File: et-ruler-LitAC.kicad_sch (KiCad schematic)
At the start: 18 parts, among them J1 Conn_01x03, SW1 SW_DPST

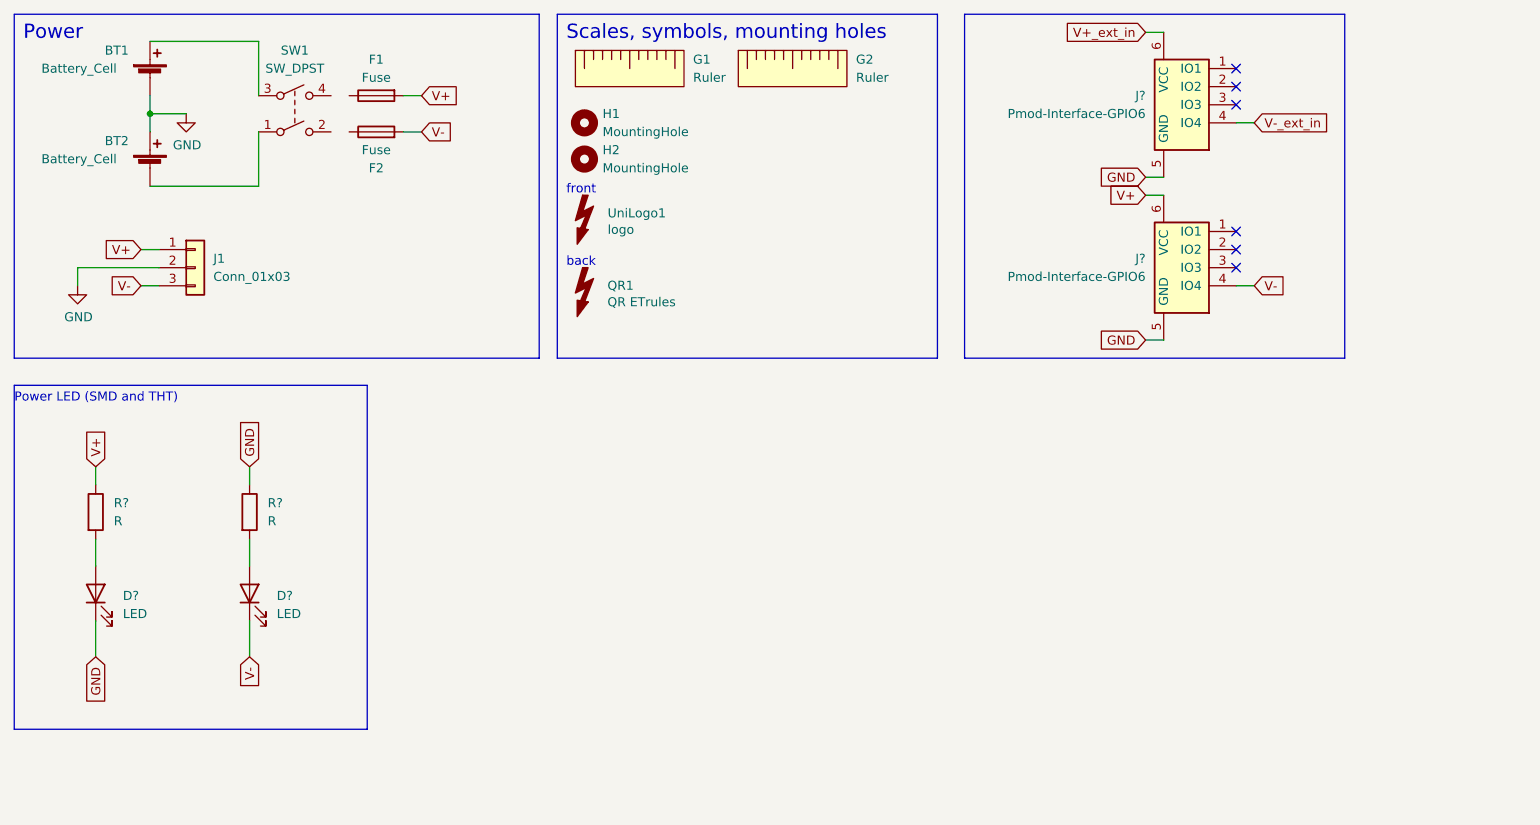
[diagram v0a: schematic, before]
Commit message: Add Converter schematic
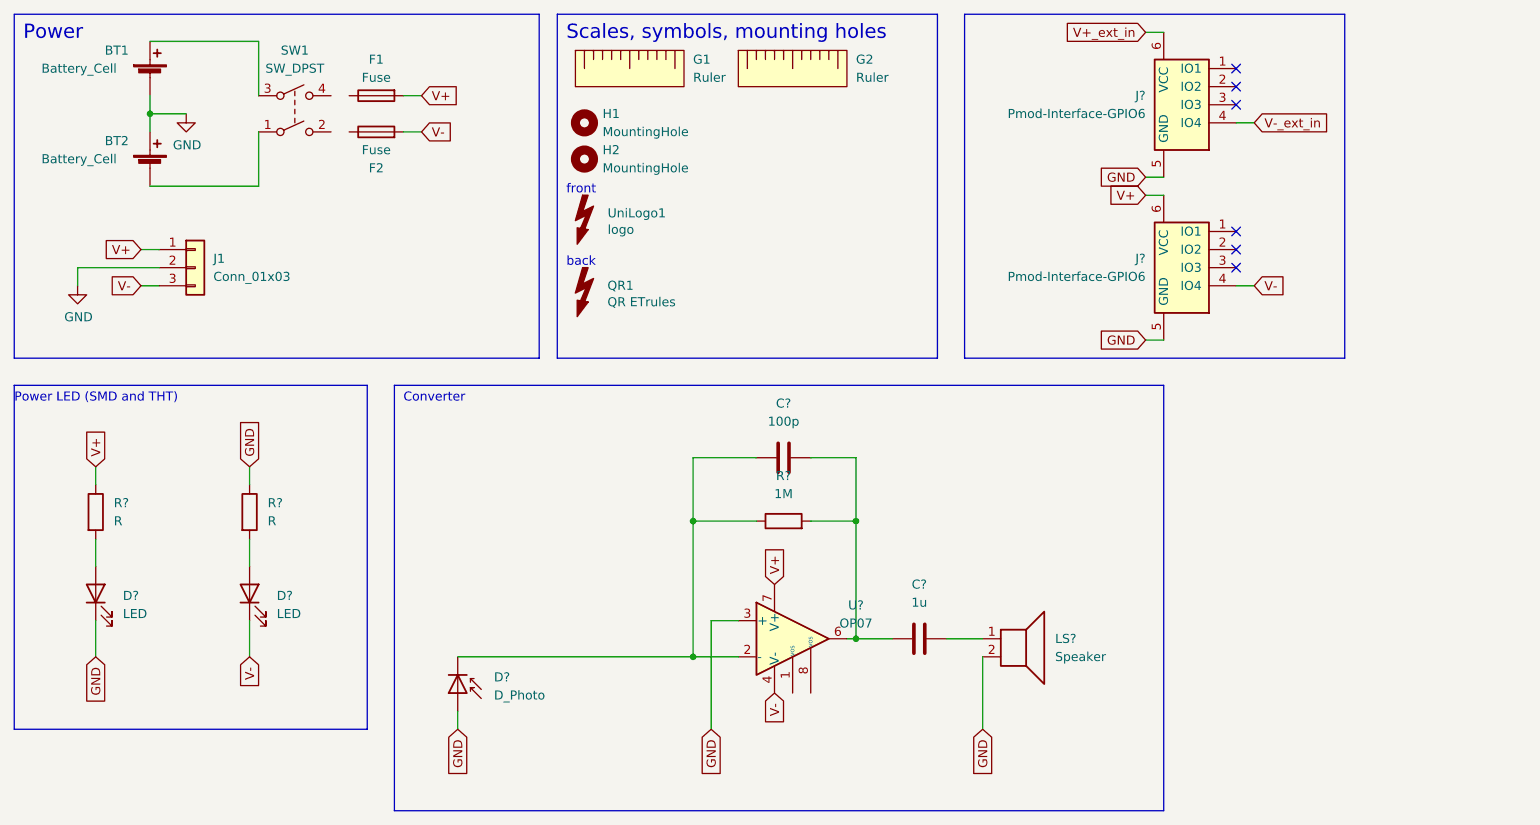
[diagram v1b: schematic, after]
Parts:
- added C?: 1u, symbol Device:C
- added C?: 100p, symbol Device:C
- added D?: D_Photo, LED_THT:LED_D5.0mm_Clear, symbol Device:D_Photo
- added LS?: Speaker, symbol Device:Speaker
- added R?: 1M, symbol Device:R
- added U?: OP07, Package_DIP:DIP-8_W7.62mm_Socket_LongPads, symbol Amplifier_Operational:OP07
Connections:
- net GND: now also D?.2 (A), LS?.2, U?.3 (+)
- net V+: now also U?.7 (V+)
- net V-: now also U?.4 (V-)
- new net: C?.1, D?.1 (K), R?.1, U?.2 (-)
- new net: C?.1, C?.2, R?.2, U?.6
- new net: C?.2, LS?.1
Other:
- note added: "Converter"

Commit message: Fix GND symbol and schematic labels
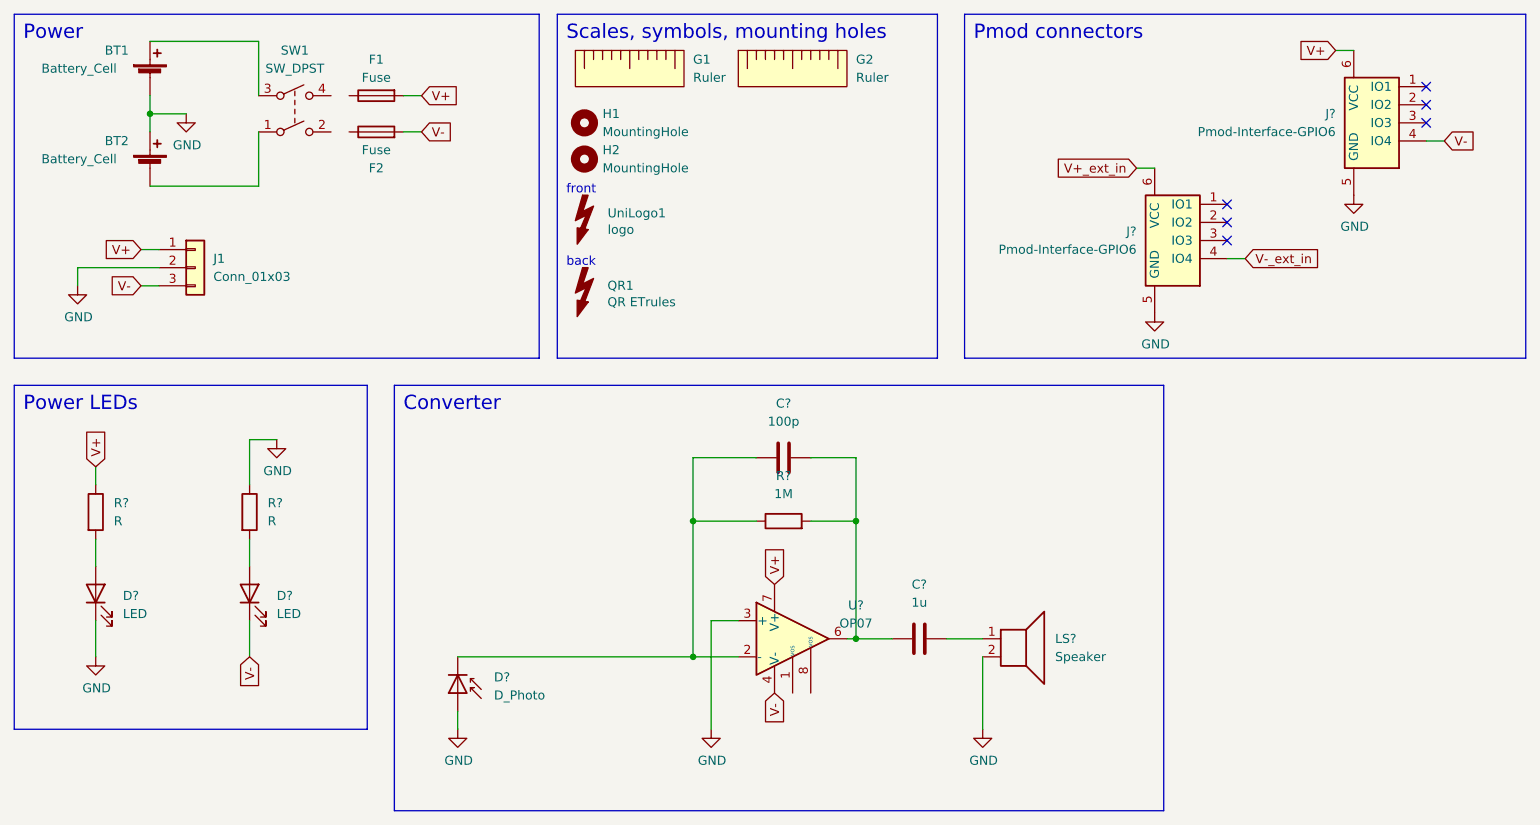
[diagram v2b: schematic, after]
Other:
- note added: "Pmod connectors"
- note added: "Power LEDs"
- note removed: "Power LED (SMD and THT)"
- moved on the sheet: J?

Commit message: Add volume control and headphone jack
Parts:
- added J?: AudioJack2, symbol Connector:AudioJack2
- added RV?: R_Potentiometer, symbol Device:R_Potentiometer
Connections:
- net GND: now also J?.T
- net at C?.2: now also RV?.1, RV?.2; no longer LS?.1
- new net: J?.S, LS?.1, RV?.3
- no-connect marks 6 -> 8
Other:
- moved on the sheet: LS?
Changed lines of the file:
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@@
   (junction (at 135.89 105.41) (diameter 0) (color 0 0 0 0)
   )
+  (junction (at 166.37 118.11) (diameter 0) (color 0 0 0 0)
+  )
+  (junction (at 168.91 105.41) (diameter 0) (color 0 0 0 0)
+  )
   (junction (at 36.83 31.75) (diameter 0) (color 0 0 0 0)
   )
   (junction (at 113.03 107.95) (diameter 0) (color 0 0 0 0)
   )
+  (junction (at 151.13 105.41) (diameter 0) (color 0 0 0 0)
+  )
+  (no_connect (at 127 113.03))
   (no_connect (at 187.96 46.99))
   (no_connect (at 215.9 33.02))
+  (no_connect (at 129.54 113.03))
   (no_connect (at 215.9 30.48))
   (no_connect (at 187.96 44.45))
@@
     (stroke (width 0) (type default) (color 0 0 0 0))
   )
-  (wire (pts (xy 148.59 105.41) (xy 153.67 105.41))
-    (stroke (width 0) (type default) (color 0 0 0 0))
-  )
-  (polyline (pts (xy 71.12 129.54) (xy 179.07 129.54))
+  (polyline (pts (xy 71.12 129.54) (xy 194.31 129.54))
     (stroke (width 0) (type default) (color 0 0 0 0))
   )
@@
     (stroke (width 0) (type default) (color 0 0 0 0))
   )
-  (polyline (pts (xy 179.07 129.54) (xy 179.07 69.85))
+  (polyline (pts (xy 194.31 129.54) (xy 194.31 69.85))
     (stroke (width 0) (type default) (color 0 0 0 0))
   )
@@
     (stroke (width 0) (type default) (color 0 0 0 0))
   )
+  (wire (pts (xy 148.59 105.41) (xy 151.13 105.41))
+    (stroke (width 0) (type default) (color 0 0 0 0))
+  )
   (polyline (pts (xy 67.31 118.11) (xy 67.31 69.85))
     (stroke (width 0) (type default) (color 0 0 0 0))
@@
     (stroke (width 0) (type default) (color 0 0 0 0))
   )
+  (wire (pts (xy 166.37 118.11) (xy 172.72 118.11))
+    (stroke (width 0) (type default) (color 0 0 0 0))
+  )
   (wire (pts (xy 113.03 88.9) (xy 113.03 107.95))
     (stroke (width 0) (type default) (color 0 0 0 0))
   )
+  (wire (pts (xy 160.02 105.41) (xy 168.91 105.41))
+    (stroke (width 0) (type default) (color 0 0 0 0))
+  )
   (wire (pts (xy 80.01 115.57) (xy 80.01 118.11))
     (stroke (width 0) (type default) (color 0 0 0 0))
@@
     (stroke (width 0) (type default) (color 0 0 0 0))
   )
+  (wire (pts (xy 151.13 105.41) (xy 152.4 105.41))
+    (stroke (width 0) (type default) (color 0 0 0 0))
+  )
+  (wire (pts (xy 168.91 105.41) (xy 172.72 105.41))
+    (stroke (width 0) (type default) (color 0 0 0 0))
+  )
   (wire (pts (xy 134.62 105.41) (xy 135.89 105.41))
     (stroke (width 0) (type default) (color 0 0 0 0))
@@
     (stroke (width 0) (type default) (color 0 0 0 0))
   )
+  (wire (pts (xy 166.37 107.95) (xy 166.37 118.11))
+    (stroke (width 0) (type default) (color 0 0 0 0))
+  )
   (wire (pts (xy 121.92 80.01) (xy 113.03 80.01))
     (stroke (width 0) (type default) (color 0 0 0 0))
@@
     (stroke (width 0) (type default) (color 0 0 0 0))
   )
+  (wire (pts (xy 168.91 115.57) (xy 172.72 115.57))
+    (stroke (width 0) (type default) (color 0 0 0 0))
+  )
   (wire (pts (xy 113.03 80.01) (xy 113.03 88.9))
     (stroke (width 0) (type default) (color 0 0 0 0))
@@
     (stroke (width 0) (type default) (color 0 0 0 0))
   )
+  (wire (pts (xy 166.37 107.95) (xy 172.72 107.95))
+    (stroke (width 0) (type default) (color 0 0 0 0))
+  )
   (polyline (pts (xy 93.98 17.78) (xy 147.32 17.78))
     (stroke (width 0) (type default) (color 0 0 0 0))
   )
-  (wire (pts (xy 153.67 107.95) (xy 153.67 118.11))
-    (stroke (width 0) (type default) (color 0 0 0 0))
-  )
   (wire (pts (xy 41.91 31.75) (xy 36.83 31.75))
     (stroke (width 0) (type default) (color 0 0 0 0))
@@
     (stroke (width 0) (type default) (color 0 0 0 0))
   )
+  (wire (pts (xy 151.13 101.6) (xy 156.21 101.6))
+    (stroke (width 0) (type default) (color 0 0 0 0))
+  )
   (polyline (pts (xy 147.32 66.04) (xy 147.32 17.78))
     (stroke (width 0) (type default) (color 0 0 0 0))
@@
     (stroke (width 0) (type default) (color 0 0 0 0))
   )
+  (wire (pts (xy 166.37 118.11) (xy 166.37 120.65))
+    (stroke (width 0) (type default) (color 0 0 0 0))
+  )
   (wire (pts (xy 36.83 21.59) (xy 52.07 21.59))
     (stroke (width 0) (type default) (color 0 0 0 0))
   )
+  (wire (pts (xy 151.13 105.41) (xy 151.13 101.6))
+    (stroke (width 0) (type default) (color 0 0 0 0))
+  )
   (wire (pts (xy 135.89 88.9) (xy 135.89 105.41))
     (stroke (width 0) (type default) (color 0 0 0 0))
   )
-  (polyline (pts (xy 179.07 69.85) (xy 71.12 69.85))
+  (polyline (pts (xy 194.31 69.85) (xy 71.12 69.85))
     (stroke (width 0) (type default) (color 0 0 0 0))
   )
   (wire (pts (xy 26.67 55.88) (xy 26.67 53.34))
+    (stroke (width 0) (type default) (color 0 0 0 0))
+  )
+  (wire (pts (xy 168.91 105.41) (xy 168.91 115.57))
     (stroke (width 0) (type default) (color 0 0 0 0))
   )
@@
     (pin "1")
   )
-  (symbol (lib_id "power:GND") (at 153.67 118.11 0) (unit 1)
-    (in_bom yes) (on_board yes)
-    (property "Reference" "#PWR?" (id 0) (at 153.67 124.46 0)
-      (effects (font (size 1.27 1.27)) hide)
-    )
-    (property "Value" "GND" (id 1) (at 153.797 122.5042 0))
-    (property "Footprint" "" (id 2) (at 153.67 118.11 0)
-      (effects (font (size 1.27 1.27)) hide)
-    )
-    (property "Datasheet" "" (id 3) (at 153.67 118.11 0)
+  (symbol (lib_id "power:GND") (at 166.37 120.65 0) (unit 1)
+    (in_bom yes) (on_board yes)
+    (property "Reference" "#PWR?" (id 0) (at 166.37 127 0)
+      (effects (font (size 1.27 1.27)) hide)
+    )
+    (property "Value" "GND" (id 1) (at 166.497 125.0442 0))
+    (property "Footprint" "" (id 2) (at 166.37 120.65 0)
+      (effects (font (size 1.27 1.27)) hide)
+    )
+    (property "Datasheet" "" (id 3) (at 166.37 120.65 0)
       (effects (font (size 1.27 1.27)) hide)
     )
@@
     (pin "1")
   )
+  (symbol (lib_id "Connector:AudioJack2") (at 177.8 118.11 0) (mirror y) (unit 1)
+    (in_bom yes) (on_board yes) (fields_autoplaced)
+    (property "Reference" "J?" (id 0) (at 182.88 116.2049 0)
+      (effects (font (size 1.27 1.27)) (justify right))
+    )
+    (property "Value" "AudioJack2" (id 1) (at 182.88 118.7449 0)
+      (effects (font (size 1.27 1.27)) (justify right))
+    )
+    (property "Footprint" "" (id 2) (at 177.8 118.11 0)
+      (effects (font (size 1.27 1.27)) hide)
+    )
+    (property "Datasheet" "~" (id 3) (at 177.8 118.11 0)
+      (effects (font (size 1.27 1.27)) hide)
+    )
+    (pin "S")
+    (pin "T")
+  )
   (symbol (lib_id "Device:C") (at 125.73 80.01 90) (unit 1)
     (in_bom yes) (on_board yes) (fields_autoplaced)
@@
     (pin "1")
   )
+  (symbol (lib_id "Device:R_Potentiometer") (at 156.21 105.41 90) (unit 1)
+    (in_bom yes) (on_board yes) (fields_autoplaced)
+    (property "Reference" "RV?" (id 0) (at 156.21 109.22 90))
+    (property "Value" "R_Potentiometer" (id 1) (at 156.21 111.76 90))
+    (property "Footprint" "" (id 2) (at 156.21 105.41 0)
+      (effects (font (size 1.27 1.27)) hide)
+    )
+    (property "Datasheet" "~" (id 3) (at 156.21 105.41 0)
+      (effects (font (size 1.27 1.27)) hide)
+    )
+    (pin "1")
+    (pin "2")
+    (pin "3")
+  )
   (symbol (lib_id "Device:R") (at 29.21 87.63 0) (unit 1)
     (in_bom yes) (on_board yes) (fields_autoplaced)
@@
     (pin "2")
   )
-  (symbol (lib_id "Device:Speaker") (at 158.75 105.41 0) (unit 1)
-    (in_bom yes) (on_board yes) (fields_autoplaced)
-    (property "Reference" "LS?" (id 0) (at 163.83 105.4099 0)
-      (effects (font (size 1.27 1.27)) (justify left))
-    )
-    (property "Value" "Speaker" (id 1) (at 163.83 107.9499 0)
-      (effects (font (size 1.27 1.27)) (justify left))
-    )
-    (property "Footprint" "" (id 2) (at 158.75 110.49 0)
-      (effects (font (size 1.27 1.27)) hide)
-    )
-    (property "Datasheet" "~" (id 3) (at 158.496 106.68 0)
+  (symbol (lib_id "Device:Speaker") (at 177.8 105.41 0) (unit 1)
+    (in_bom yes) (on_board yes) (fields_autoplaced)
+    (property "Reference" "LS?" (id 0) (at 182.88 105.4099 0)
+      (effects (font (size 1.27 1.27)) (justify left))
+    )
+    (property "Value" "Speaker" (id 1) (at 182.88 107.9499 0)
+      (effects (font (size 1.27 1.27)) (justify left))
+    )
+    (property "Footprint" "" (id 2) (at 177.8 110.49 0)
+      (effects (font (size 1.27 1.27)) hide)
+    )
+    (property "Datasheet" "~" (id 3) (at 177.546 106.68 0)
       (effects (font (size 1.27 1.27)) hide)
     )
@@
       (reference "J?") (unit 1) (value "Pmod-Interface-GPIO6") (footprint "emt-pmod:Pmod_Interface_Male6")
     )
+    (path "/6bd42537-1769-423f-b89f-3db96fb6df12"
+      (reference "J?") (unit 1) (value "AudioJack2") (footprint "")
+    )
     (path "/6e691bf6-0efc-402a-ba4f-a200826ebb05"
       (reference "J?") (unit 1) (value "Pmod-Interface-GPIO6") (footprint "emt-pmod:Pmod_Interface_Female6")
@@
       (reference "R?") (unit 1) (value "R") (footprint "et-ruler-footprints:R_0805_THT_10.16mm_Hybrid")
     )
+    (path "/bc33b1c6-079a-49a3-8116-ecc3d5bd5b09"
+      (reference "RV?") (unit 1) (value "R_Potentiometer") (footprint "")
+    )
     (path "/0c91bcd3-285e-47fd-acbd-2bedce603d40"
